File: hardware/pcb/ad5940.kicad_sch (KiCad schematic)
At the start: 31 parts, among them J6 EDA pads, U7 AD5940BCBZ-RL7

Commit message: Fix the review's datasheet errors without changing respiration or the GDTs.
Replace the MCP73831 with a BQ25170 so a flat cell still charges from USB, add the missing series protection and ESP32/CP2102 passives, and withdraw the claim that respiration still works with 51 kΩ in the loop.

Co-authored-by: Riyu-D1 <Riyu-D1@users.noreply.github.com>
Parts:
- added R76, R77, R78, R79: 51k, Resistor_SMD:R_2512_6332Metric, symbol vitalq:R
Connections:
- net CE0: now also R39.2; no longer R39.1
- net CE_ISO: now also C54.2, R39.1; no longer C54.1, R39.2
- net DE0: now also R42.2; no longer D9.1, R42.1
- net EDA_CE_PAD: now also R76.1; no longer C54.2
- net EDA_DE_PAD: now also R79.1; no longer R42.2
- net EDA_RE_PAD: now also R78.1; no longer R41.2
- net EDA_SE_PAD: now also R77.1; no longer R40.2
- net RE0: now also R41.2; no longer D8.1, R41.1
- net SE0: now also C55.2; no longer C55.1
- net SE_ISO: now also C55.1, R40.2; no longer C55.2, R40.1
- new net CE_SURGE: C54.1, R76.2
- new net DE_SURGE: D9.1, R42.1, R79.2
- new net RE_SURGE: D8.1, R41.1, R78.2
- new net SE_SURGE: R40.1, R77.2
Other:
- note added: "R76-R79 are the pad-side 51k DPCR. C54 sits behind R76. R39 stays the 1k RLIMIT."
- note removed: "RLIMIT is R39. CISO1 is C54. CISO2 is C55. R13 stays the 1k RCAL. D17-D20 are on the pads."

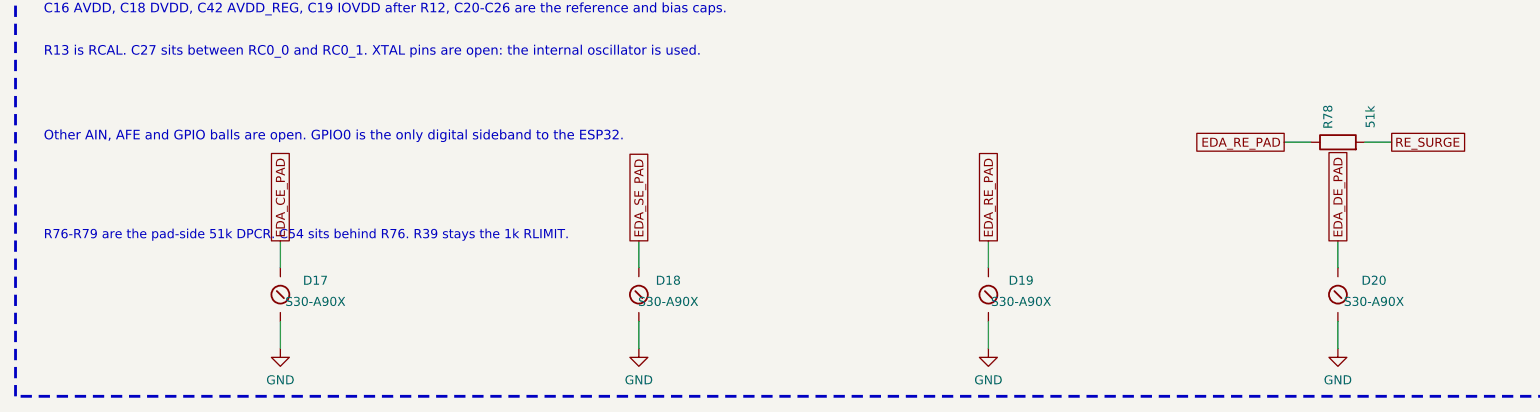
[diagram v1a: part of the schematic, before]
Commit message: Remove the gas-discharge tubes and pack the board to 36.5 by 45.6 mm.
D12-D20 and the S30 footprint are gone. Each patient line is now pad, 51 kΩ DPCR, TPD1E10B06, then the series resistor into the IC. A fourth creepage slot fills the gap the last tube was blocking.

Co-authored-by: Riyu-D1 <Riyu-D1@users.noreply.github.com>
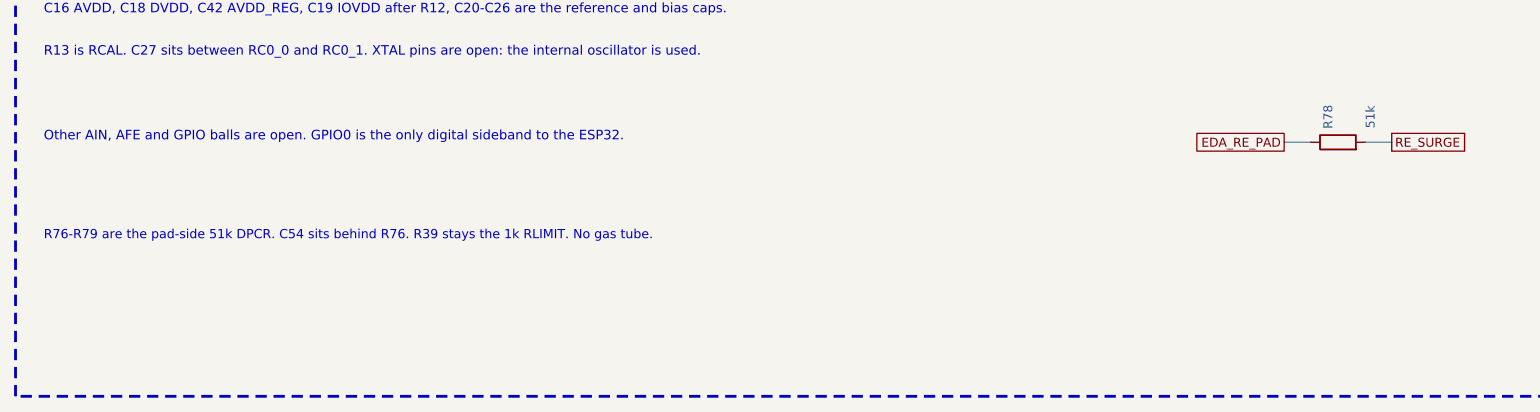
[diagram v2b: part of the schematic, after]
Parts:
- removed D17, D18, D19, D20: S30-A90X, vitalq:GDT_S30, symbol vitalq:GDT
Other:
- note added: "R76-R79 are the pad-side 51k DPCR. C54 sits behind R76. R39 stays the 1k RLIMIT. No gas tube."
- note removed: "R76-R79 are the pad-side 51k DPCR. C54 sits behind R76. R39 stays the 1k RLIMIT."

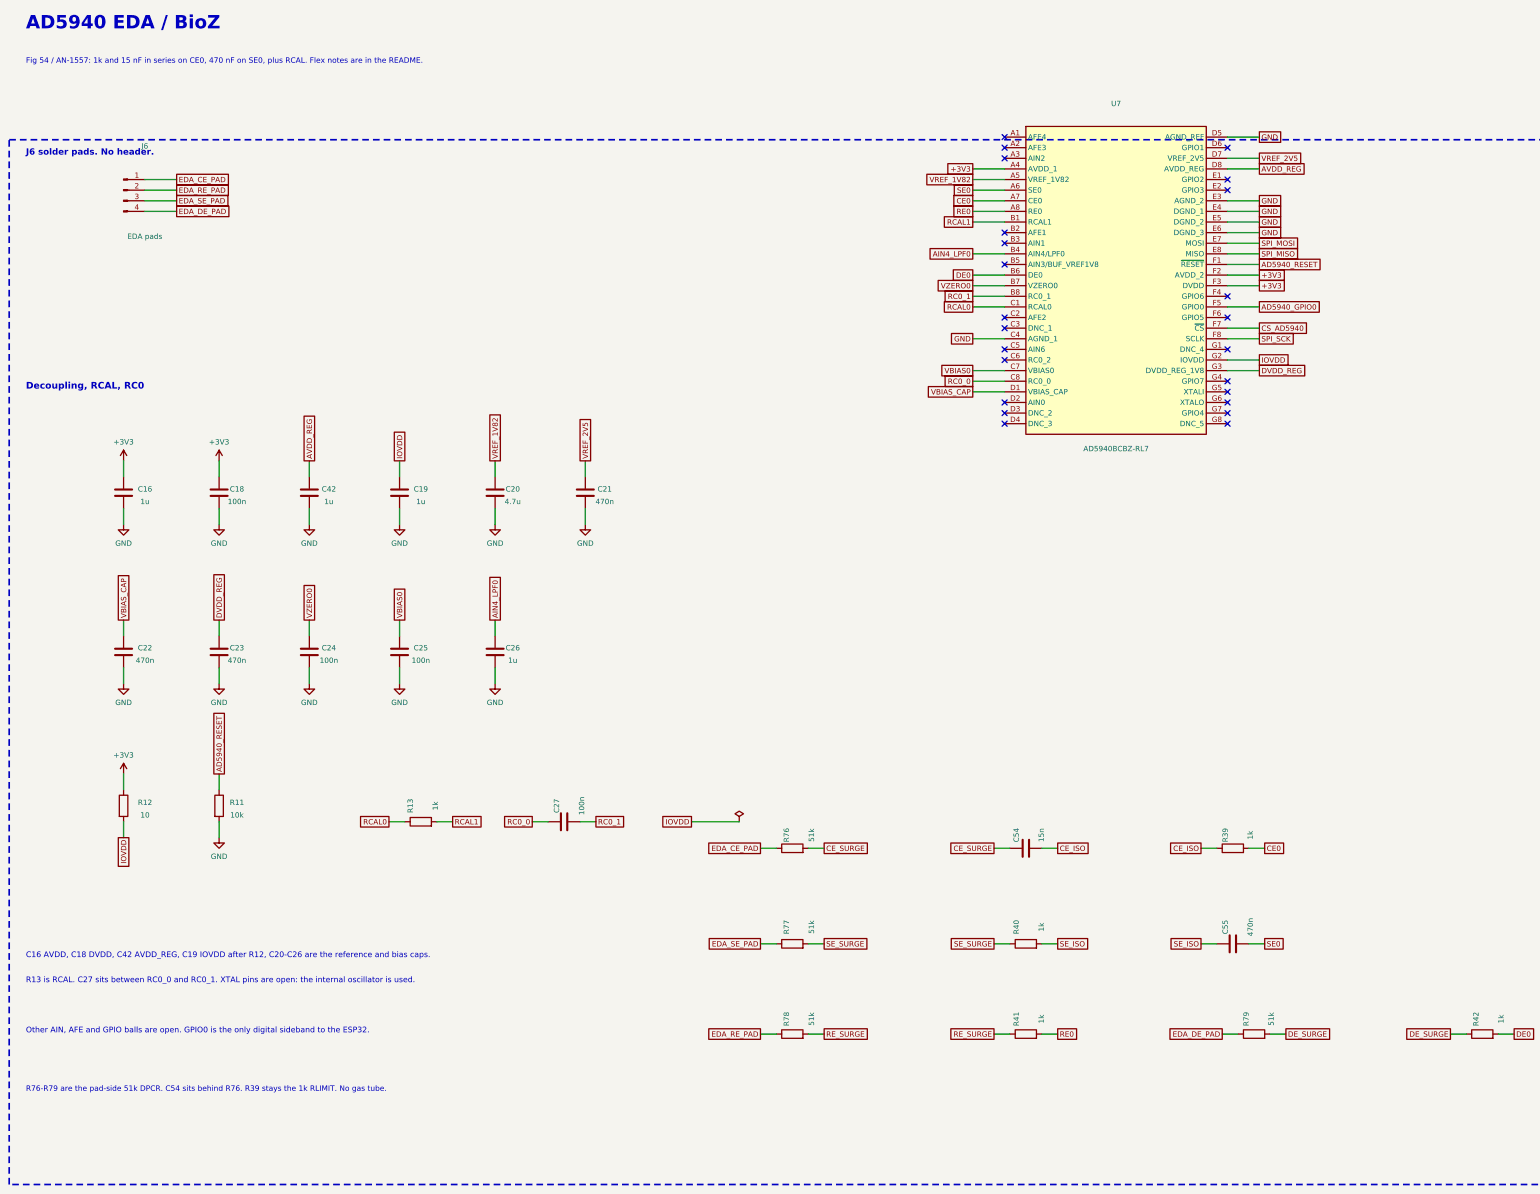
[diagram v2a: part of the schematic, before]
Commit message: Add a 4-wire chest respiration path on the AD5940.
The ADS1292R modulation network stays. Chest breathing uses four dedicated pads into AIN1, AIN0, AIN3, and AIN2, with the same pad-side surge chain and the datasheet isolation capacitors. Shoulder EDA remains on CE0, SE0, RE0, and DE0.

Co-authored-by: Riyu-D1 <Riyu-D1@users.noreply.github.com>
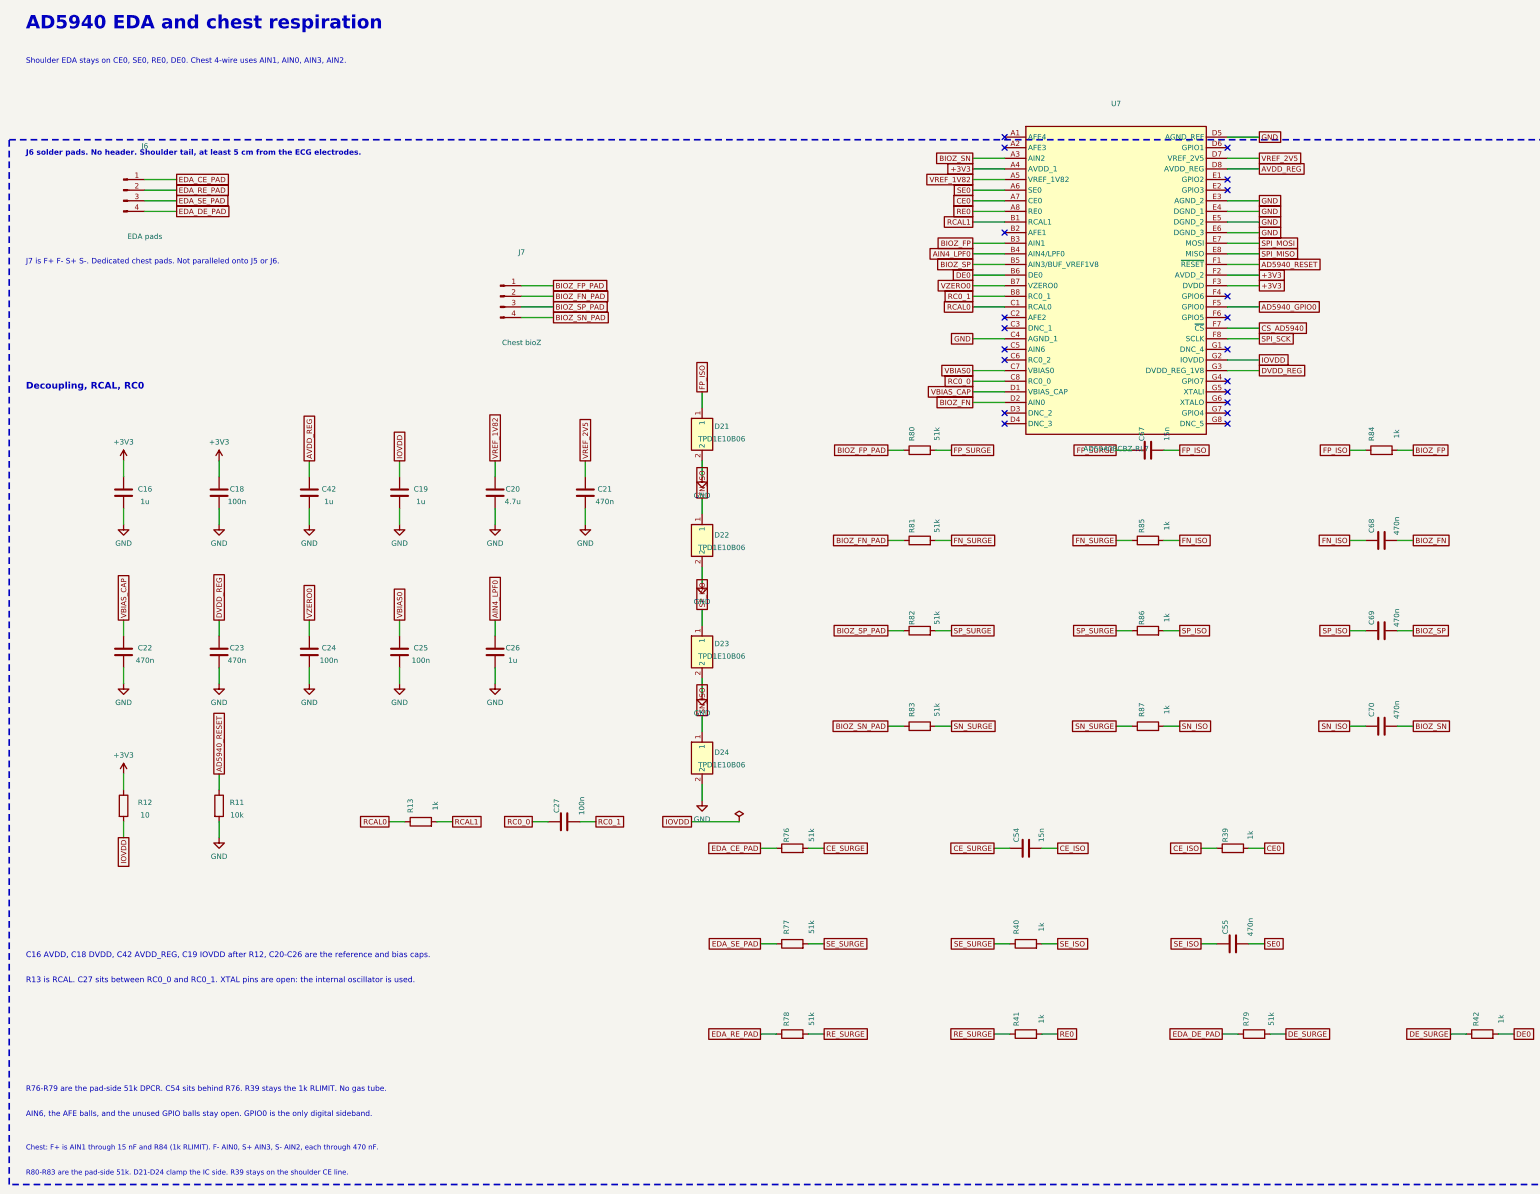
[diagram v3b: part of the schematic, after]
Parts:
- added C67: 15n, Capacitor_SMD:C_0402_1005Metric, symbol vitalq:C
- added C68, C69, C70: 470n, Capacitor_SMD:C_0402_1005Metric, symbol vitalq:C
- added D21, D22, D23, D24: TPD1E10B06, vitalq:TPD1E10B06_DPY, symbol vitalq:D_TVS_2
- added J7: Chest bioZ, vitalq:Pads_BIOZ, symbol vitalq:Conn_01x04_Pin
- added R80, R81, R82, R83: 51k, Resistor_SMD:R_2512_6332Metric, symbol vitalq:R
- added R84, R85, R86, R87: 1k, Resistor_SMD:R_0402_1005Metric, symbol vitalq:R
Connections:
- net GND: now also D21.2, D22.2, D23.2, D24.2
- net BIOZ_SN: now reaches U7.A3 (AIN2)
- net BIOZ_SN: now also C70.2
- net BIOZ_FP: now reaches U7.B3 (AIN1)
- net BIOZ_FP: now also R84.2
- net BIOZ_SP: now reaches U7.B5 (AIN3/BUF_VREF1V8)
- net BIOZ_SP: now also C69.2
- net BIOZ_FN: now reaches U7.D2 (AIN0)
- net BIOZ_FN: now also C68.2
- new net BIOZ_FN_PAD: J7.2 (Pin_2), R81.1
- new net BIOZ_FP_PAD: J7.1 (Pin_1), R80.1
- new net BIOZ_SN_PAD: J7.4 (Pin_4), R83.1
- new net BIOZ_SP_PAD: J7.3 (Pin_3), R82.1
- new net FN_ISO: C68.1, D22.1, R85.2
- new net FN_SURGE: R81.2, R85.1
- new net FP_ISO: C67.2, D21.1, R84.1
- new net FP_SURGE: C67.1, R80.2
- new net SN_ISO: C70.1, D24.1, R87.2
- new net SN_SURGE: R83.2, R87.1
- new net SP_ISO: C69.1, D23.1, R86.2
- new net SP_SURGE: R82.2, R86.1
- no-connect marks 24 -> 20
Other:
- note added: "AD5940 EDA and chest respiration"
- note added: "AIN6, the AFE balls, and the unused GPIO balls stay open. GPIO0 is the only digital sideband."
- note added: "Chest: F+ is AIN1 through 15 nF and R84 (1k RLIMIT). F- AIN0, S+ AIN3, S- AIN2, each through 470 nF."
- note added: "J6 solder pads. No header. Shoulder tail, at least 5 cm from the ECG electrodes."
- note added: "J7 is F+ F- S+ S-. Dedicated chest pads. Not paralleled onto J5 or J6."
- note added: "R80-R83 are the pad-side 51k. D21-D24 clamp the IC side. R39 stays on the shoulder CE line."
- note added: "Shoulder EDA stays on CE0, SE0, RE0, DE0. Chest 4-wire uses AIN1, AIN0, AIN3, AIN2."
- note removed: "AD5940 EDA / BioZ"
- note removed: "Fig 54 / AN-1557: 1k and 15 nF in series on CE0, 470 nF on SE0, plus RCAL. Flex notes are in the README."
- note removed: "J6 solder pads. No header."
- note removed: "Other AIN, AFE and GPIO balls are open. GPIO0 is the only digital sideband to the ESP32."

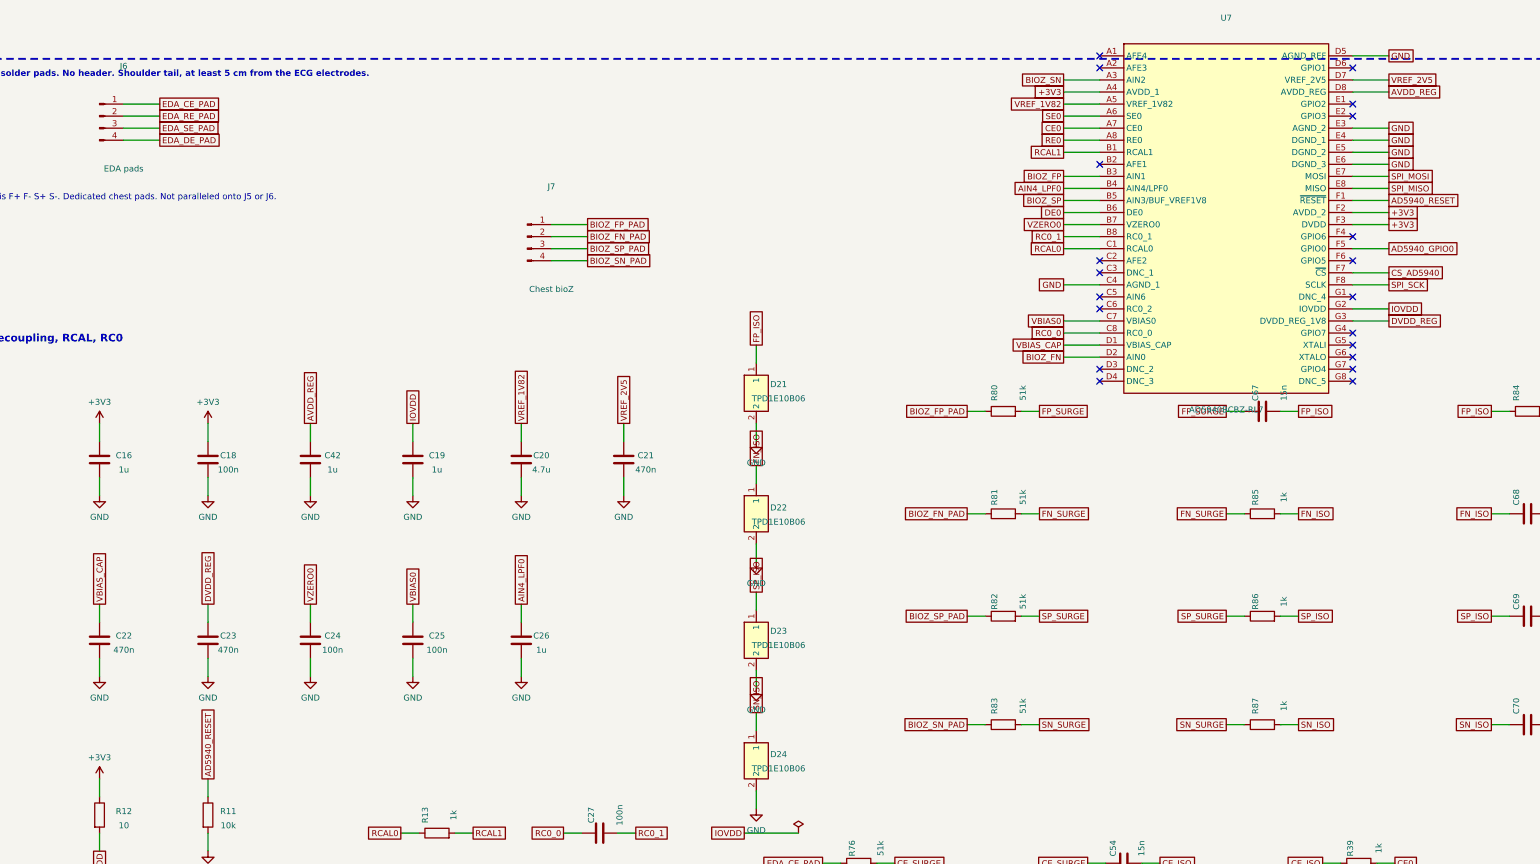
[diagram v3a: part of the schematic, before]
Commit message: Prepare hw_v1 for prefab review without claiming the route is finished.
Add the gauge TDFN, USB ESD, sense links, test access, and JLC BOM fields, and keep the partial Freerouting result with the remaining open nets listed.

Co-authored-by: Riyu-D1 <Riyu-D1@users.noreply.github.com>
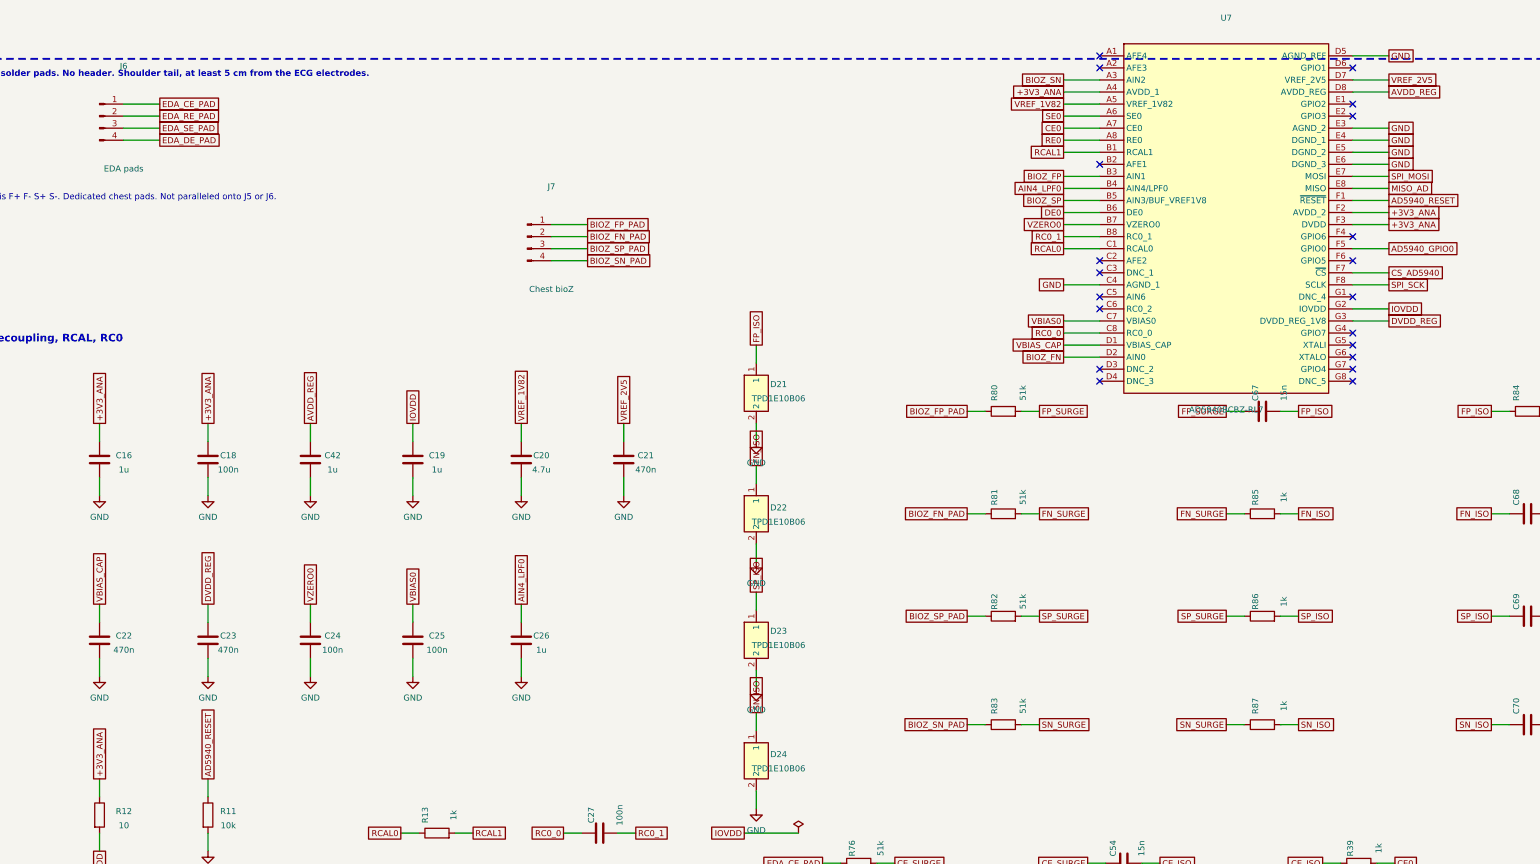
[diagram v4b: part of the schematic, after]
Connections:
- net +3V3 renamed +3V3_ANA
- net SPI_MISO renamed MISO_AD
